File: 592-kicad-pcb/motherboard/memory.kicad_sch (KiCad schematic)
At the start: 15 parts, among them J19 Micro_SD_Card, J20 Conn_02x01, U13 W25Q32JVSS, U14 SN74LVC1G3157DBVR

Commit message: update jlcpcb part numbers
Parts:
- R48, R49: footprint (none) -> Resistor_SMD:R_0402_1005Metric; LCSC (none) -> C25741
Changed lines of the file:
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@@
 			)
 		)
-		(property "Footprint" ""
+		(property "Footprint" "Resistor_SMD:R_0402_1005Metric"
 			(at 55.88 118.11 0)
 			(effects
@@
 		)
 		(property "Description" "Resistor, small symbol"
+			(at 55.88 118.11 0)
+			(effects
+				(font
+					(size 1.27 1.27)
+				)
+				(hide yes)
+			)
+		)
+		(property "LCSC" "C25741"
 			(at 55.88 118.11 0)
 			(effects
@@
 			)
 		)
-		(property "Footprint" ""
+		(property "Footprint" "Resistor_SMD:R_0402_1005Metric"
 			(at 60.96 53.34 0)
 			(effects
@@
 			(at 60.96 53.34 0)
 			(effects
+				(font
+					(size 1.27 1.27)
+				)
+				(hide yes)
+			)
+		)
+		(property "LCSC" "C25741"
+			(at 60.96 53.34 0)
+			(effects

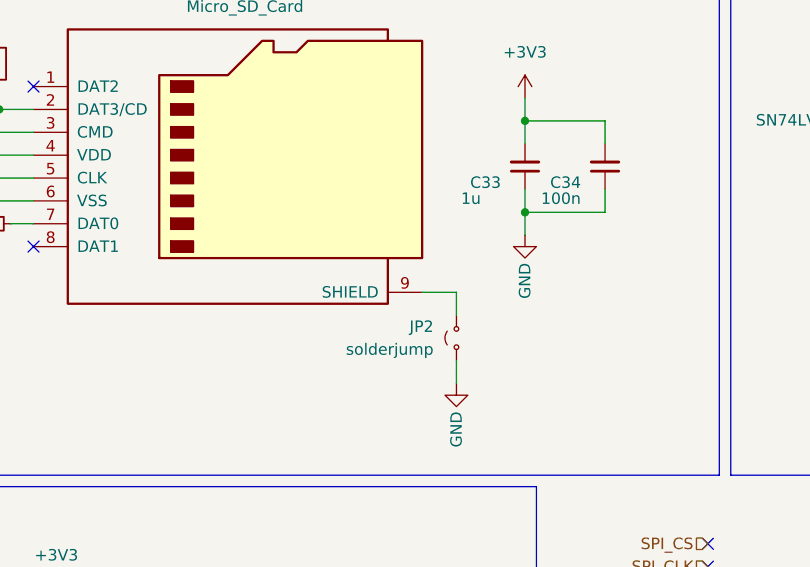
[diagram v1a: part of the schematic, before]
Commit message: further routing progess: core routing done
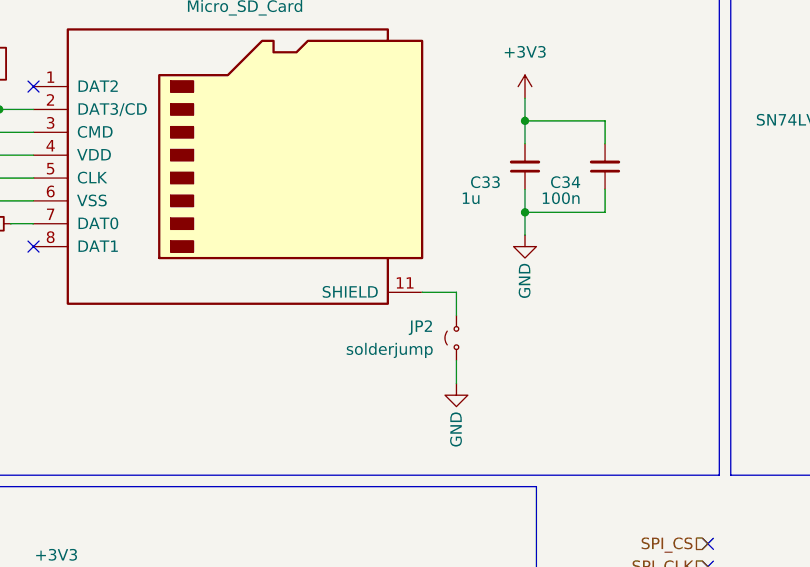
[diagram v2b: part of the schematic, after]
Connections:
- net at JP2.2 (B): now also J19.11 (SHIELD); no longer J19.9 (SHIELD)
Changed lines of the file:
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@@
 		(pin "1"
 		)
-		(pin "9"
+		(pin "11"
 		)
 		(pin "8"

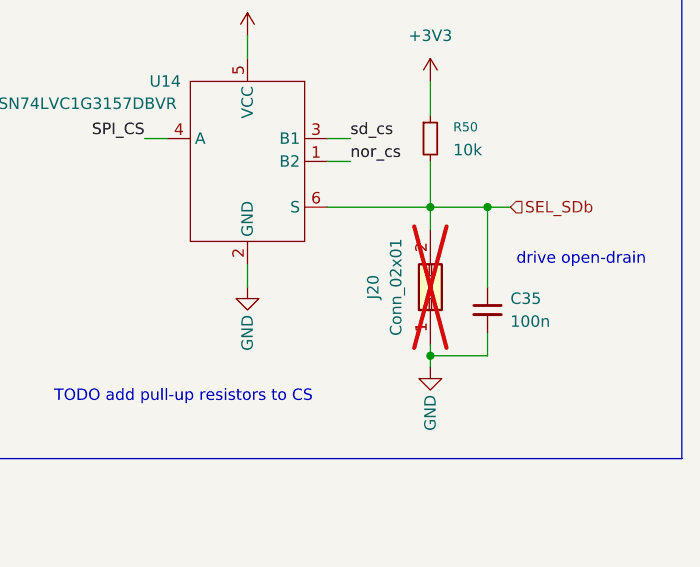
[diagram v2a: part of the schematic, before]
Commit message: complete routing for core
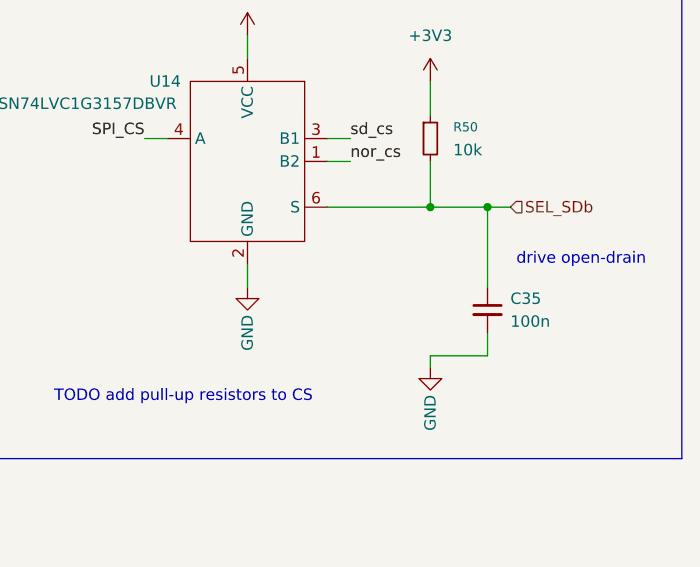
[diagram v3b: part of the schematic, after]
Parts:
- removed J20: Conn_02x01, Connector_PinHeader_1.27mm:PinHeader_1x02_P1.27mm_Vertical, symbol Connector_Generic:Conn_02x01
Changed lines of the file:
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@@
-	)
-	(junction
-		(at 193.04 87.63)
-		(diameter 0)
-		(color 0 0 0 0)
 	)
 	(junction
@@
 	(wire
 		(pts
-			(xy 193.04 73.66) (xy 193.04 71.12)
-		)
-		(stroke
-			(width 0)
-			(type default)
-		)
-	)
-	(wire
-		(pts
 			(xy 46.99 66.04) (xy 64.77 66.04)
 		)
@@
 		(pts
 			(xy 119.38 67.31) (xy 119.38 69.85)
-		)
-		(stroke
-			(width 0)
-			(type default)
-		)
-	)
-	(wire
-		(pts
-			(xy 193.04 87.63) (xy 193.04 86.36)
 		)
 		(stroke
@@
 					(unit 1)
 				)
-			)
-		)
-	)
-	(symbol
-		(lib_id "Connector_Generic:Conn_02x01")
-		(at 193.04 81.28 90)
-		(unit 1)
-		(exclude_from_sim no)
-		(in_bom yes)
-		(on_board yes)
-		(dnp yes)
-		(fields_autoplaced yes)
-		(property "Reference" "J20"
-			(at 186.69 80.01 0)
-			(effects
-				(font
-					(size 1.27 1.27)
-				)
-			)
-		)
-		(property "Value" "Conn_02x01"
-			(at 189.23 80.01 0)
-			(effects
-				(font
-					(size 1.27 1.27)
-				)
-			)
-		)
-		(property "Footprint" "Connector_PinHeader_1.27mm:PinHeader_1x02_P1.27mm_Vertical"
-			(at 193.04 81.28 0)
-			(effects
-				(font
-					(size 1.27 1.27)
-				)
-				(hide yes)
-			)
-		)
-		(property "Datasheet" "~"
-			(at 193.04 81.28 0)
-			(effects
-				(font
-					(size 1.27 1.27)
-				)
-				(hide yes)
-			)
-		)
-		(property "Description" "Generic connector, double row, 02x01, this symbol is compatible with counter-clockwise, top-bottom and odd-even numbering schemes., script generated (kicad-library-utils/schlib/autogen/connector/)"
-			(at 193.04 81.28 0)
-			(effects
-				(font
-					(size 1.27 1.27)
-				)
-				(hide yes)
-			)
-		)
-		(property "Characteristics" ""
-			(at 193.04 81.28 0)
-			(effects
-				(font
-					(size 1.27 1.27)
-				)
-				(hide yes)
-			)
-		)
-		(property "DigikeyPN" ""
-			(at 193.04 81.28 0)
-			(effects
-				(font
-					(size 1.27 1.27)
-				)
-				(hide yes)
-			)
-		)
-		(property "MPN" ""
-			(at 193.04 81.28 0)
-			(effects
-				(font
-					(size 1.27 1.27)
-				)
-				(hide yes)
-			)
-		)
-		(property "MPN_ALT" ""
-			(at 193.04 81.28 0)
-			(effects
-				(font
-					(size 1.27 1.27)
-				)
-				(hide yes)
-			)
-		)
-		(property "Manufacturer" ""
-			(at 193.04 81.28 0)
-			(effects
-				(font
-					(size 1.27 1.27)
-				)
-				(hide yes)
-			)
-		)
-		(property "Variant" ""
-			(at 193.04 81.28 0)
-			(effects
-				(font
-					(size 1.27 1.27)
-				)
-				(hide yes)
-			)
-		)
-		(property "Vendor" ""
-			(at 193.04 81.28 0)
-			(effects
-				(font
-					(size 1.27 1.27)
-				)
-				(hide yes)
-			)
-		)
-		(pin "1"
-		)
-		(pin "2"
-		)
-		(instances
-			(project "motherboard"
-				(path "/5b0c97ac-fa03-4db8-b41b-0eee32b6f55d/f049e4ad-bebe-4338-850a-2727de737ae9/2022d8e8-455b-4f4a-b4b4-f79e7486e2af"
-					(reference "J20")
-					(unit 1)
-				)
